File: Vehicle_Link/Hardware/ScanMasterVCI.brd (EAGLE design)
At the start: 53 x 39.4 mm, 90 parts, among them IC1 XMEGA32A4U, Q1 MMBT4403, Q10 ZXMP6A17G, Q11 MMBT3904, Q12 MMBT3904, Q2 MMBT3904, Q3 MMBT3904, Q4 MMBT3904, Q5 MMBT3904, Q6 MMBT3904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

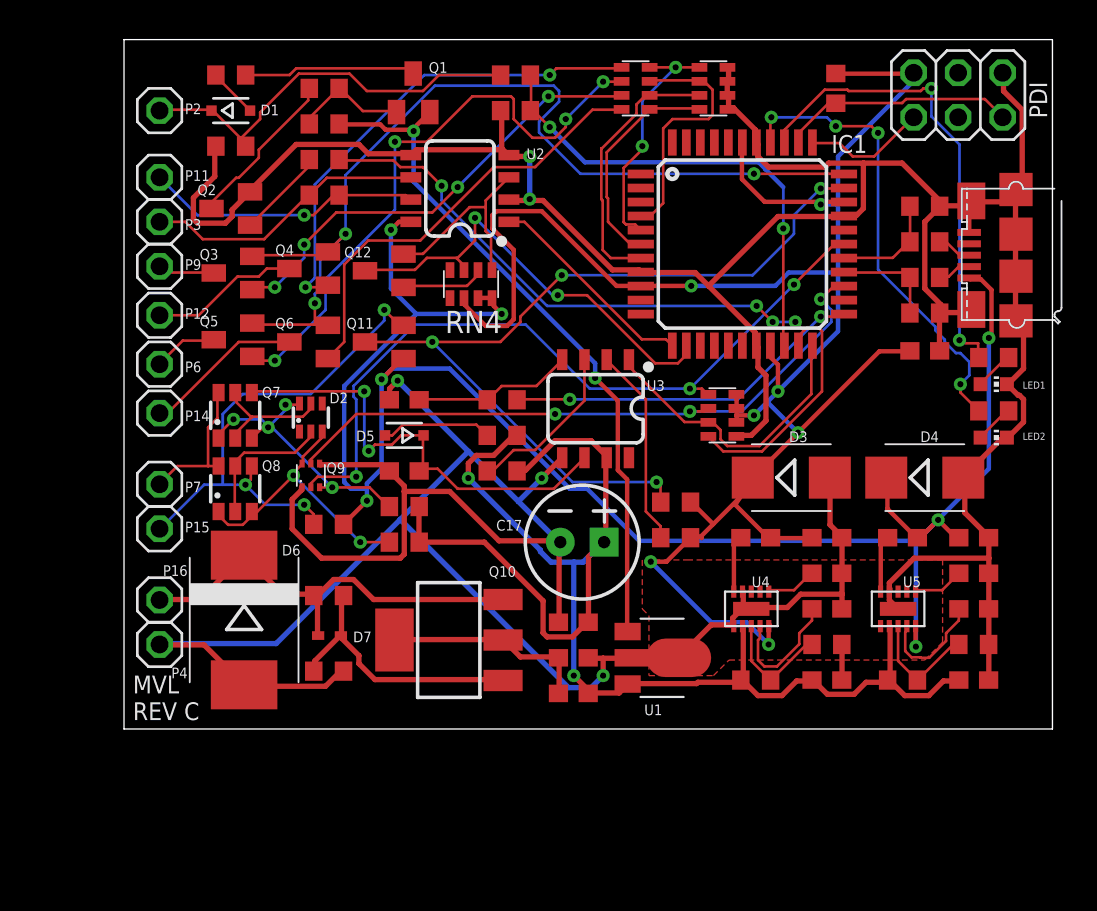
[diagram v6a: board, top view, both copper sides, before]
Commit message: Made some landing pad changes to the voltage IC's, to fix heat issues I saw. Started looking into simplifying the circuit to get rid of some of the vias.
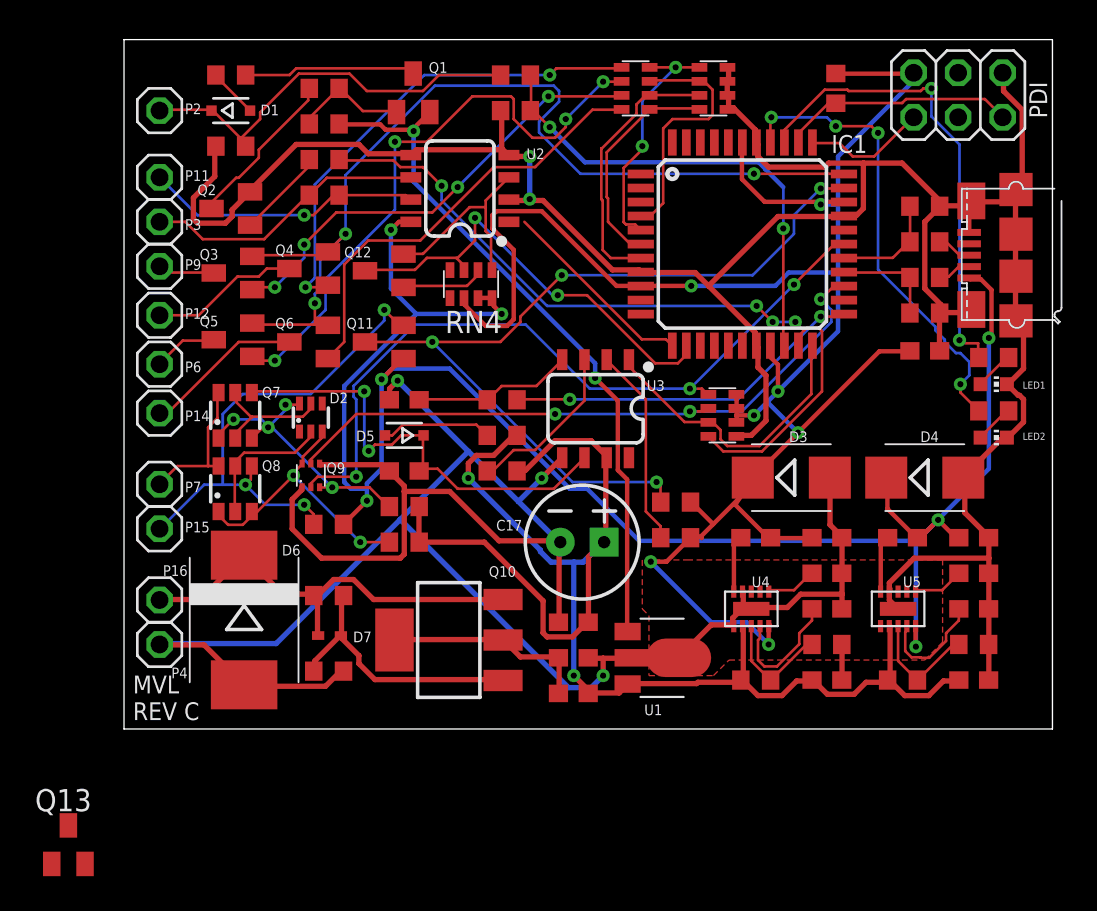
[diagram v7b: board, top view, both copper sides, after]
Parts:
- added Q13: MMBT3904, semicon-smd-ipc:SOT23
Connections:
- new net N$34: Q13.2, U2.1
- new net N$35: Q13.1, RN4.4
- net +5V: now also RN4.5
- net CCD-RX: now also Q13.3; no longer U2.1
- net CCD-TX: now also Q12.2; no longer Q12.3
- net N$32: now also Q12.3; no longer Q12.2
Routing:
- net CCD-RX: track 12.3 -> 11.4 mm
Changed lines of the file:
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@@
 <attribute name="OC_NEWARK" value="unknown" x="19.812" y="25.4" size="1.778" layer="27" rot="R180" display="off"/>
 </element>
+<element name="Q13" library="semicon-smd-ipc" library_urn="urn:adsk.eagle:library:353" package="SOT23" package3d_urn="urn:adsk.eagle:package:26310/1" value="MMBT3904" x="-3.175" y="-6.604"/>
 </elements>
 <signals>
 <signal name="CCD-RX">
 <contactref element="IC1" pad="12"/>
-<contactref element="U2" pad="1"/>
-<wire x1="22.86" y1="28.956" x2="21.977" y2="28.956" width="0.1524" layer="1"/>
 <wire x1="29.5656" y1="22.2504" x2="22.86" y2="28.956" width="0.1524" layer="1"/>
 <wire x1="30.9372" y1="22.2504" x2="29.5656" y2="22.2504" width="0.1524" layer="1"/>
 <wire x1="31.242" y1="21.9456" x2="30.9372" y2="22.2504" width="0.1524" layer="1"/>
 <wire x1="31.242" y1="21.9456" x2="31.306" y2="21.886" width="0.1524" layer="1"/>
+<contactref element="Q13" pad="3"/>
+<wire x1="-3.175" y1="-5.504" x2="29.5656" y2="22.2504" width="0" layer="19" extent="1-1"/>
 </signal>
 <signal name="CCD-TX">
 <contactref element="IC1" pad="13"/>
-<contactref element="Q12" pad="3"/>
 <contactref element="RN4" pad="3"/>
 <wire x1="19.3548" y1="26.5176" x2="19.3548" y2="26.2128" width="0.1524" layer="1"/>
@@
 <wire x1="13.7922" y1="26.2128" x2="16.6116" y2="26.2128" width="0.1524" layer="1"/>
 <wire x1="19.3548" y1="26.2128" x2="19.412" y2="26.2" width="0.1524" layer="1"/>
-<wire x1="13.7922" y1="26.2128" x2="13.759" y2="26.162" width="0.1524" layer="1"/>
 <wire x1="32.0802" y1="21.336" x2="32.0802" y2="21.8694" width="0.1524" layer="1"/>
 <wire x1="31.623" y1="20.8788" x2="32.0802" y2="21.336" width="0.1524" layer="1"/>
@@
 <via x="24.765" y="24.765" extent="1-16" drill="0.35"/>
 <via x="20.0406" y="29.1846" extent="1-16" drill="0.35"/>
+<contactref element="Q12" pad="2"/>
+<wire x1="16.6116" y1="26.2128" x2="15.959" y2="27.112" width="0" layer="19" extent="1-1"/>
 </signal>
 <signal name="SCI-RX">
@@
 <via x="21.5646" y="23.6982" extent="1-16" drill="0.35"/>
 <via x="15.24" y="28.4988" extent="1-16" drill="0.35"/>
+<contactref element="RN4" pad="5"/>
+<wire x1="20.212" y1="24.6" x2="18.612" y2="24.6" width="0" layer="19" extent="1-1"/>
 </signal>
 <signal name="J1962-16" class="1">
@@
 </signal>
 <signal name="N$32">
-<contactref element="Q12" pad="2"/>
 <contactref element="U2" pad="3"/>
 <contactref element="RN4" pad="1"/>
@@
 <wire x1="19.7358" y1="29.7942" x2="17.0688" y2="27.1272" width="0.1524" layer="1"/>
 <wire x1="20.6502" y1="29.7942" x2="19.7358" y2="29.7942" width="0.1524" layer="1"/>
-<wire x1="16.002" y1="27.1272" x2="15.959" y2="27.112" width="0.1524" layer="1"/>
+<contactref element="Q12" pad="3"/>
+<wire x1="13.759" y1="26.162" x2="16.002" y2="27.1272" width="0" layer="19" extent="1-1"/>
 </signal>
 <signal name="N$33">
@@
 <wire x1="16.002" y1="25.2222" x2="15.959" y2="25.212" width="0.1524" layer="1"/>
 </signal>
+<signal name="N$34">
+<contactref element="Q13" pad="2"/>
+<contactref element="U2" pad="1"/>
+<wire x1="-2.225" y1="-7.704" x2="21.977" y2="28.956" width="0" layer="19" extent="1-1"/>
+</signal>
+<signal name="N$35">
+<contactref element="Q13" pad="1"/>
+<contactref element="RN4" pad="4"/>
+<wire x1="-4.125" y1="-7.704" x2="18.612" y2="26.2" width="0" layer="19" extent="1-1"/>
+</signal>
 </signals>

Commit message: Re-routed the entire board to try and reduce the number of vias
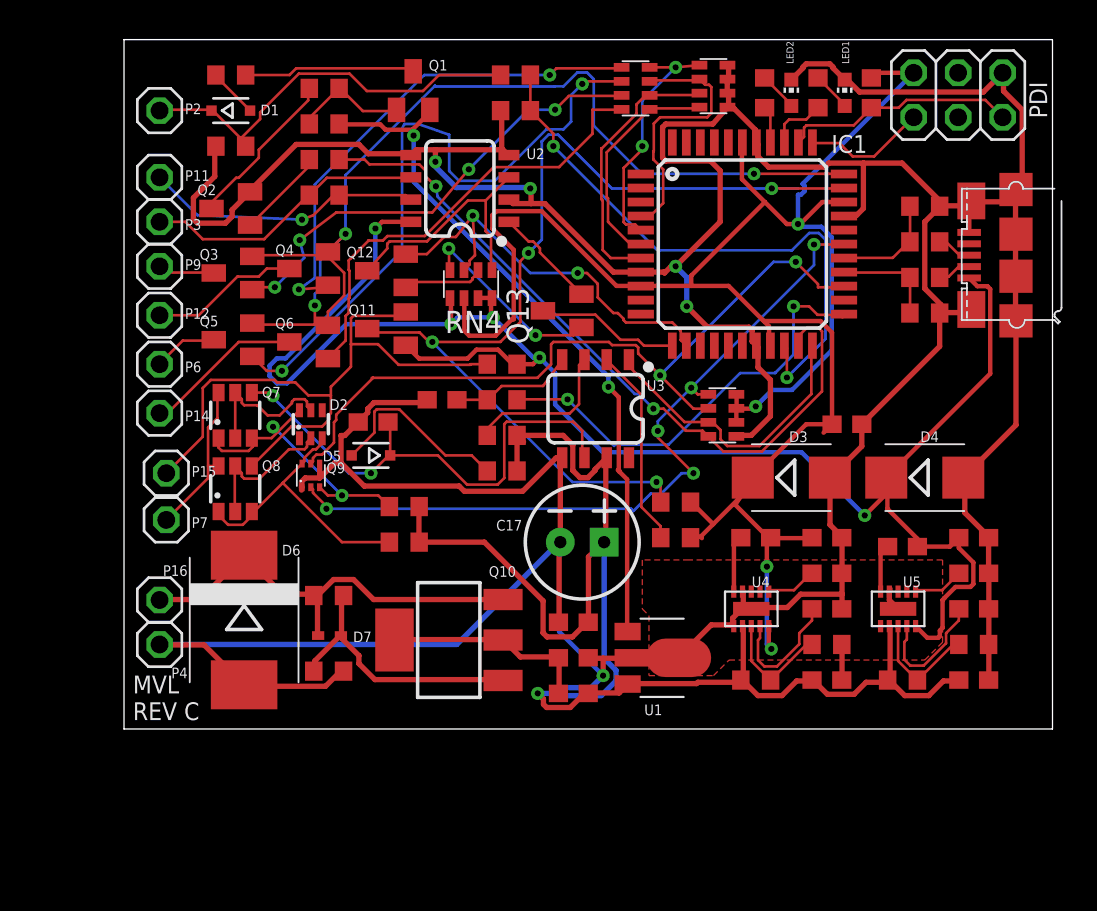
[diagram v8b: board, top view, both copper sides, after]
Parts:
- moved Q13 41.5 mm to (25.0, 23.9), turned to 90 degrees
- moved LED2 22.8 mm to (38.1, 36.3), turned to 0 degrees
- moved R30 22.4 mm to (36.6, 36.3), turned to 270 degrees
- moved LED1 18.7 mm to (41.1, 36.3), turned to 0 degrees
- moved R24 18.1 mm to (39.6, 36.3), turned to 270 degrees
- moved R16 13.5 mm to (21.6, 20.8)
- moved C3 6.11 mm to (41.3, 17.4)
- moved C5 3.31 mm to (14.2, 17.5)
- moved P15 3.20 mm to (2.41, 14.6)
- moved D5 2.22 mm to (14.1, 15.6)
- moved C4 2.16 mm to (18.2, 18.8)
- moved P7 2.07 mm to (2.41, 11.9)
- moved R29 2.05 mm to (42.7, 36.3)
- moved R14 2.03 mm to (21.6, 16.8)
- moved R17 2.03 mm to (21.6, 14.7)
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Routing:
- net COM-LED: track 26.8 -> 2.12 mm, vias 4 -> 0
- net PWR-LED: track 27.2 -> 3.35 mm, vias 2 -> 0
- net N$35: track 0.00 -> 11.2 mm, vias 0 -> 2
- net GND: track 282.1 -> 292.1 mm
- net SCI-RX: track 49.2 -> 58.0 mm
- net J1962-15: track 29.9 -> 37.0 mm, vias 3 -> 0
- net J1850VPW-RX: track 27.5 -> 33.8 mm
- net N$34: track 0.00 -> 6.00 mm
- net ISO-K-EN: track 37.5 -> 43.0 mm, vias 3 -> 2
- net ISO-K-TX: track 20.7 -> 25.4 mm
- net +5V: track 104.4 -> 99.7 mm, vias 7 -> 5
- net N$31: track 6.34 -> 11.0 mm
- net SCI-TX: track 55.1 -> 59.3 mm
- net N$21: track 34.0 -> 37.1 mm, vias 4 -> 2
- net CCD-RX: track 11.4 -> 8.30 mm
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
